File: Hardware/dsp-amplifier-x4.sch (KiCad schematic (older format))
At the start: 35 parts, among them J1 Raspberry_Pi_2_3, J3 USBi, P1 Conn_WallPlug_Earth, Q1 STD2805, U1 ADAU1452

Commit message: various fixes
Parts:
- added C42, C43, C44, C48, C49, C50, C55, C57, C60, C61: 10n, Capacitor_SMD:C_0805_2012Metric_Pad1.18x1.45mm_HandSolder, symbol dsp-amplifier-x4-rescue:Capacitor
- added C45, C46, C47, C51, C52, C53, C58, C59, C62, C63: 100n, Capacitor_SMD:C_0805_2012Metric_Pad1.18x1.45mm_HandSolder, symbol dsp-amplifier-x4-rescue:Capacitor
- added J4, J5: Screw_Terminal_01x02, TerminalBlock:TerminalBlock_Altech_AK300-2_P5.00mm, symbol Connector:Screw_Terminal_01x02
- added R38, R39, R40: 33, Resistor_SMD:R_0603_1608Metric_Pad0.98x0.95mm_HandSolder, symbol Device:R
- added R41, R44: 4.3k, Resistor_SMD:R_0603_1608Metric_Pad0.98x0.95mm_HandSolder, symbol Device:R
- added R42, R43: DNP, Resistor_SMD:R_0603_1608Metric_Pad0.98x0.95mm_HandSolder, symbol Device:R
- added RV1, RV2: R_POT, Potentiometer_THT:Potentiometer_Vishay_248GJ-249GJ_Single_Vertical, symbol Device:R_POT
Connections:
- net labels added: AMP1_BCLK, AMP1_NSPK_SD, AMP1_SPK_SLEEP, AMP2_BCLK, AMP2_NSPK_SD, AMP2_SPK_SLEEP, EXT_I_BCLK, EXT_I_SDATA, EXT_O_BCLK, EXT_O_LRCLK, EXT_O_SDIN, GAIN0, GAIN1, VDRIVE, VPOT0, VPOT1
- net labels removed: AMP1_SCLK, AMP2_SCLK
- wire segments 171 -> 294
- no-connect marks 15 -> 18
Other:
- moved on the sheet: C21, C22, C23, C24, C28, FB1, J1, Q1, R1, R9

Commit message: started routing
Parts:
- removed C42, C43, C48, C49, C50, C55, C57, C60, C61: 10n, Capacitor_SMD:C_0805_2012Metric_Pad1.18x1.45mm_HandSolder, symbol dsp-amplifier-x4-rescue:Capacitor
- removed C45, C46, C51, C52, C53, C58, C59, C62, C63: 100n, Capacitor_SMD:C_0805_2012Metric_Pad1.18x1.45mm_HandSolder, symbol dsp-amplifier-x4-rescue:Capacitor
- removed P1: Conn_WallPlug_Earth, symbol Connector:Conn_WallPlug_Earth
- removed R16, R38, R39: 33, Resistor_SMD:R_0603_1608Metric_Pad0.98x0.95mm_HandSolder, symbol Device:R
- added C10, C11, C14, C15, C16, C20, C21, C3, C4: 10n, Capacitor_SMD:C_0603_1608Metric_Pad1.08x0.95mm_HandSolder, symbol Device:C
- added C12, C13, C17, C18, C19, C23, C24, C7, C8: 100n, Capacitor_SMD:C_0603_1608Metric_Pad1.08x0.95mm_HandSolder, symbol Device:C
- added F1: Fuse, Fuse:Fuseholder_Cylinder-5x20mm_Stelvio-Kontek_PTF78_Horizontal_Open, symbol Device:Fuse
- added J2: EXT, Connector_PinHeader_2.54mm:PinHeader_2x08_P2.54mm_Vertical, symbol Connector_Generic:Conn_02x08_Odd_Even
- added J6, J7: Screw_Terminal_01x02, TerminalBlock:TerminalBlock_Wuerth_691311400102_P7.62mm, symbol Connector:Screw_Terminal_01x02
- added P1: Conn_WallPlug, symbol Connector:Conn_WallPlug
- added R23, R24, R25, R26: 33, Resistor_SMD:R_0603_1608Metric_Pad0.98x0.95mm_HandSolder, symbol Device:R
- C1: renamed from C21; value 4.7u -> 10u; footprint Capacitor_SMD:C_0805_2012Metric_Pad1.18x1.45mm_HandSolder -> Capacitor_SMD:C_1206_3216Metric_Pad1.33x1.80mm_HandSolder; symbol dsp-amplifier-x4-rescue:Capacitor -> Device:C
- C22: renamed from C23; value 4.7u -> 10u; footprint Capacitor_SMD:C_0805_2012Metric_Pad1.18x1.45mm_HandSolder -> Capacitor_SMD:C_1206_3216Metric_Pad1.33x1.80mm_HandSolder; symbol dsp-amplifier-x4-rescue:Capacitor -> Device:C
- C25: renamed from C24; value 4.7u -> 10u; footprint Capacitor_SMD:C_0805_2012Metric_Pad1.18x1.45mm_HandSolder -> Capacitor_SMD:C_1206_3216Metric_Pad1.33x1.80mm_HandSolder; symbol dsp-amplifier-x4-rescue:Capacitor -> Device:C
- C26: renamed from C28; value 4.7u -> 10u; footprint Capacitor_SMD:C_0805_2012Metric_Pad1.18x1.45mm_HandSolder -> Capacitor_SMD:C_1206_3216Metric_Pad1.33x1.80mm_HandSolder; symbol dsp-amplifier-x4-rescue:Capacitor -> Device:C
- C27: renamed from C22; value 4.7u -> 10u; footprint Capacitor_SMD:C_0805_2012Metric_Pad1.18x1.45mm_HandSolder -> Capacitor_SMD:C_1206_3216Metric_Pad1.33x1.80mm_HandSolder; symbol dsp-amplifier-x4-rescue:Capacitor -> Device:C
- C5: renamed from C44; footprint Capacitor_SMD:C_0805_2012Metric_Pad1.18x1.45mm_HandSolder -> Capacitor_SMD:C_0603_1608Metric_Pad1.08x0.95mm_HandSolder; symbol dsp-amplifier-x4-rescue:Capacitor -> Device:C
- C9: renamed from C47; footprint Capacitor_SMD:C_0805_2012Metric_Pad1.18x1.45mm_HandSolder -> Capacitor_SMD:C_0603_1608Metric_Pad1.08x0.95mm_HandSolder; symbol dsp-amplifier-x4-rescue:Capacitor -> Device:C
- FB1: footprint Inductor_SMD:L_0805_2012Metric_Pad1.05x1.20mm_HandSolder -> Inductor_SMD:L_0603_1608Metric_Pad1.05x0.95mm_HandSolder
- J4, J5: footprint TerminalBlock:TerminalBlock_Altech_AK300-2_P5.00mm -> TerminalBlock:TerminalBlock_Wuerth_691311400102_P7.62mm
- renumbered C19 to C2, C20 to C6, J3 to J1, J1 to J3, R14 to R1, R25 to R10, R26 to R11, R27 to R12, R9 to R13, R28 to R14, R32 to R15, R33 to R16, R34 to R17, R35 to R18, R36 to R19, R15 to R2, R29 to R20, R30 to R21, R31 to R22, R41 to R27, R42 to R28, R43 to R29, R17 to R3, R44 to R30, R1 to R4, R21 to R5, R40 to R6, R22 to R7, R23 to R8, R24 to R9
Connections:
- net labels added: EXT_BCLK, EXT_LRCLK, EXT_MCLK, EXT_MDI, EXT_MDO, SCL, SDA
- net labels removed: EXT_I_BCLK, EXT_I_SDATA, EXT_O_BCLK, EXT_O_LRCLK, EXT_O_SDIN
- wire segments 294 -> 334
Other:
- moved on the sheet: C2, C6, FB1, J1, J3, J4, J5, Q1, R1, R13, R14, R15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

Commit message: routing progress
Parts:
- removed R21: 33, Resistor_SMD:R_0603_1608Metric_Pad0.98x0.95mm_HandSolder, symbol Device:R
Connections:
- net AMP1_CLOCK: now also R25.2; no longer R23.2
- net DSP_CLOCK: now also R23.2; no longer R25.2
- net PI_SDATA_I: now also J3.38 (GPIO20/MOSI1)
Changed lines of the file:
@@
 PI_SDATA_I
-Wire Wire Line
-	8000 7550 8700 7550
 Wire Wire Line
 	9600 1000 9350 1000
@@
 Text Label 11550 2050 2    60   ~ 0
 AMP2_CLOCK
+Text Label 11550 2250 2    60   ~ 0
+AMP1_CLOCK
 Text Label 11550 1850 2    60   ~ 0
-AMP1_CLOCK
-Text Label 11550 2250 2    60   ~ 0
 DSP_CLOCK
 Wire Wire Line
@@
 $EndComp
 $Comp
-L Device:R R21
-U 1 1 60BB796A
-P 8850 7550
-F 0 "R21" V 8643 7550 50  0001 C CNN
-F 1 "33" V 8734 7550 50  0001 C CNN
-F 2 "Resistor_SMD:R_0603_1608Metric_Pad0.98x0.95mm_HandSolder" V 8780 7550 50  0001 C CNN
-F 3 "~" H 8850 7550 50  0001 C CNN
-	1    8850 7550
-	0    1    1    0
-$EndComp
-$Comp
 L Device:R R22
 U 1 1 60BB7970
@@
 Wire Wire Line
 	9000 7450 9050 7450
-Wire Wire Line
-	9050 7550 9000 7550
 Wire Wire Line
 	9000 7650 9050 7650
@@
 Wire Wire Line
 	10550 2050 10500 2050
+Wire Wire Line
+	8000 7550 9050 7550
 $EndSCHEMATC

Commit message: routing, added 4 layers
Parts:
- J3: footprint Connector_PinHeader_2.54mm:PinHeader_2x20_P2.54mm_Vertical -> rpi_socket:PinSocket_2x20_P2.54mm_Vertical
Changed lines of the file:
@@
 F 0 "J3" H 9850 9131 50  0000 C CNN
 F 1 "Raspberry_Pi_2_3" H 9850 9040 50  0000 C CNN
-F 2 "Connector_PinHeader_2.54mm:PinHeader_2x20_P2.54mm_Vertical" H 9850 7650 50  0001 C CNN
+F 2 "rpi_socket:PinSocket_2x20_P2.54mm_Vertical" H 9850 7650 50  0001 C CNN
 F 3 "https://www.raspberrypi.org/documentation/hardware/raspberrypi/schematics/rpi_SCH_3bplus_1p0_reduced.pdf" H 9850 7650 50  0001 C CNN
 	1    9850 7650
@@
 Text Label 8000 7450 0    60   ~ 0
 PI_LRCLK
-Text Label 8350 7250 0    60   ~ 0
-PI_BCLK
 Text Label 8000 7650 0    60   ~ 0
 PI_SDATA_O
@@
 	10150 9000 10150 8950
 Connection ~ 10050 9000
-$Comp
-L power:+5VD #PWR033
-U 1 1 6086659C
-P 9650 6050
-F 0 "#PWR033" H 9650 5900 50  0001 C CNN
-F 1 "+5VD" H 9665 6223 50  0000 C CNN
-F 2 "" H 9650 6050 50  0001 C CNN
-F 3 "" H 9650 6050 50  0001 C CNN
-	1    9650 6050
-	1    0    0    -1
-$EndComp
-Wire Wire Line
-	9650 6050 9650 6300
 Wire Wire Line
 	9750 6350 9750 6300
 Wire Wire Line
 	9750 6300 9650 6300
-Connection ~ 9650 6300
 Wire Wire Line
 	9650 6300 9650 6350
@@
 Text Label 8350 8350 0    60   ~ 0
 PI_MUTE
-Text Label 8350 7150 0    60   ~ 0
-DSP_NRESET
 Text Label 8350 8150 0    60   ~ 0
 DSP_SELFBOOT
@@
 	1400 4550 2600 4550
 Wire Wire Line
-	8350 7150 9050 7150
-Wire Wire Line
-	8350 7250 9050 7250
-Wire Wire Line
 	8000 7450 8700 7450
 Wire Wire Line
@@
 Wire Wire Line
 	8000 7550 9050 7550
+Wire Wire Line
+	8350 7250 9050 7250
+Wire Wire Line
+	8350 7150 9050 7150
+Text Label 8350 7150 0    60   ~ 0
+DSP_NRESET
+Text Label 8350 7250 0    60   ~ 0
+PI_BCLK
+Connection ~ 9650 6300
+$Comp
+L power:+5VD #PWR033
+U 1 1 6086659C
+P 9650 6050
+F 0 "#PWR033" H 9650 5900 50  0001 C CNN
+F 1 "+5VD" H 9665 6223 50  0000 C CNN
+F 2 "" H 9650 6050 50  0001 C CNN
+F 3 "" H 9650 6050 50  0001 C CNN
+	1    9650 6050
+	1    0    0    -1
+$EndComp
+Wire Wire Line
+	9650 6050 9650 6300
 $EndSCHEMATC

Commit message: complete
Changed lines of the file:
@@
 PI_SDATA_I
-Wire Wire Line
-	9600 1000 9350 1000
 Wire Wire Line
 	9350 1000 9350 950
@@
 	14050 1400 14050 1350
 Connection ~ 14050 1350
-$Comp
-L Device:Fuse F1
-U 1 1 607081C8
-P 9750 1000
-F 0 "F1" V 9553 1000 50  0000 C CNN
-F 1 "Fuse" V 9644 1000 50  0000 C CNN
-F 2 "Fuse:Fuseholder_Cylinder-5x20mm_Stelvio-Kontek_PTF78_Horizontal_Open" V 9680 1000 50  0001 C CNN
-F 3 "~" H 9750 1000 50  0001 C CNN
-	1    9750 1000
-	0    1    1    0
-$EndComp
-Wire Wire Line
-	9950 1000 9900 1000
-Wire Wire Line
-	9350 1100 9950 1100
 $Sheet
 S 13050 4000 1400 1400
@@
 Wire Wire Line
 	9650 6050 9650 6300
+Wire Wire Line
+	9950 1000 9900 1000
+$Comp
+L Device:Fuse F1
+U 1 1 607081C8
+P 9750 1000
+F 0 "F1" V 9553 1000 50  0000 C CNN
+F 1 "Fuse" V 9644 1000 50  0000 C CNN
+F 2 "Fuse:Fuseholder_Cylinder-5x20mm_Stelvio-Kontek_PTF78_Horizontal_Open" V 9680 1000 50  0001 C CNN
+F 3 "~" H 9750 1000 50  0001 C CNN
+	1    9750 1000
+	0    1    1    0
+$EndComp
+Wire Wire Line
+	9350 1000 9600 1000
+Wire Wire Line
+	9950 1100 9350 1100
 $EndSCHEMATC

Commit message: bugfixes, made smaller
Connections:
- no-connect marks 18 -> 22
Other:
- note added: "GAIN[1:0]\n00: 12.9 V full-scale\n01: 15.1 V full-scale\n10: 25.15 V full-scale\n11: Software-controlled"
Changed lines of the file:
@@
 Wire Wire Line
 	9950 1100 9350 1100
+NoConn ~ 10500 1750
+NoConn ~ 10500 1950
+NoConn ~ 10500 2150
+NoConn ~ 10500 2350
+Text Notes 14450 1100 0    60   ~ 0
+GAIN[1:0]\n00: 12.9 V full-scale\n01: 15.1 V full-scale\n10: 25.15 V full-scale\n11: Software-controlled
 $EndSCHEMATC

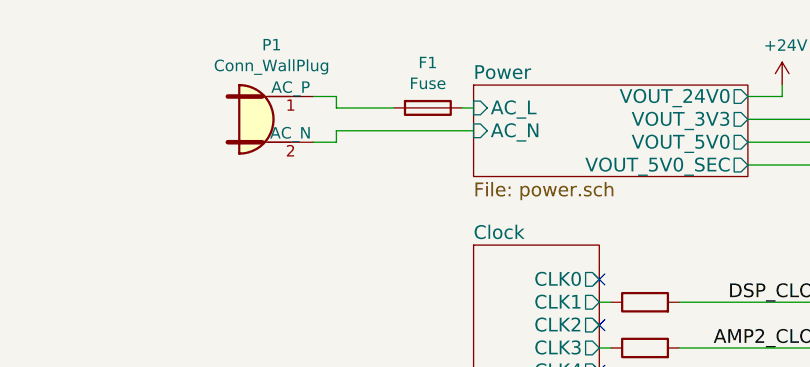
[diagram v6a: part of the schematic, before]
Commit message: connector for ac
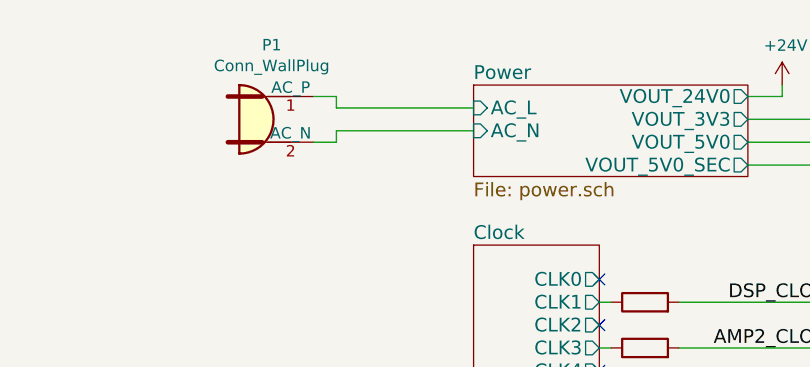
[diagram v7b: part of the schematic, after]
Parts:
- removed F1: Fuse, Fuse:Fuseholder_Cylinder-5x20mm_Stelvio-Kontek_PTF78_Horizontal_Open, symbol Device:Fuse
- P1: footprint (none) -> TerminalBlock:TerminalBlock_Wuerth_691311400102_P7.62mm
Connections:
- net Power/AC_L: now also P1.1 (AC_P)
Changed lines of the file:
@@
 F 0 "P1" H 9067 1375 50  0000 C CNN
 F 1 "Conn_WallPlug" H 9067 1284 50  0000 C CNN
-F 2 "" H 9450 1050 50  0001 C CNN
+F 2 "TerminalBlock:TerminalBlock_Wuerth_691311400102_P7.62mm" H 9450 1050 50  0001 C CNN
 F 3 "~" H 9450 1050 50  0001 C CNN
 	1    9050 1050
@@
 	9650 6050 9650 6300
 Wire Wire Line
-	9950 1000 9900 1000
-$Comp
-L Device:Fuse F1
-U 1 1 607081C8
-P 9750 1000
-F 0 "F1" V 9553 1000 50  0000 C CNN
-F 1 "Fuse" V 9644 1000 50  0000 C CNN
-F 2 "Fuse:Fuseholder_Cylinder-5x20mm_Stelvio-Kontek_PTF78_Horizontal_Open" V 9680 1000 50  0001 C CNN
-F 3 "~" H 9750 1000 50  0001 C CNN
-	1    9750 1000
-	0    1    1    0
-$EndComp
-Wire Wire Line
-	9350 1000 9600 1000
-Wire Wire Line
 	9950 1100 9350 1100
 NoConn ~ 10500 1750
@@
 Text Notes 14450 1100 0    60   ~ 0
 GAIN[1:0]\n00: 12.9 V full-scale\n01: 15.1 V full-scale\n10: 25.15 V full-scale\n11: Software-controlled
+Wire Wire Line
+	9350 1000 9950 1000
 $EndSCHEMATC

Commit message: style fixes, spi/i2c
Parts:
- removed R15, R16, R18: 4.3k, Resistor_SMD:R_0603_1608Metric_Pad0.98x0.95mm_HandSolder, symbol Device:R
- removed R17, R19: 4.3k DNP, Resistor_SMD:R_0603_1608Metric_Pad0.98x0.95mm_HandSolder, symbol Device:R
- R14: value 4.3k -> 33
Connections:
- net DSP_ADDR0 is gone; now on net PI_NCE0: U1.33 (SS/ADDR0)
- net DSP_ADDR1 is gone; now on net PI_MOSI0: U1.32 (MOSI/ADDR1)
- net +3V3: no longer R14.2
- net AMP1_NSPK_SD: now also U1.39 (LRCLK_OUT0/MP4); no longer U1.26 (SS_M/MP0)
- net AMP1_SPK_SLEEP: now also U1.42 (LRCLK_OUT1/MP5); no longer U1.27 (MOSI_M/MP1)
- net DSP_SELFBOOT: now also J3.15 (GPIO22); no longer J3.22 (GPIO25)
- net PI_BCLK: now also R14.2; no longer J3.12 (GPIO18/PWM0)
- net PI_MISO0: now also J1.5 (Pin_5), U1.30 (MISO/SDA)
- net PI_MOSI0: now also J1.8 (Pin_8)
- net PI_MUTE: now also U1.69 (LRCLK_IN3/MP13)
- net PI_NCE0: now also J1.9 (Pin_9)
- net PI_SCLK0: now also J1.7 (Pin_7), U1.31 (SCLK/SCL)
- net EEPROM_SCL: no longer names the net of R14.1
- net EEPROM_SCL: now also J3.12 (GPIO18/PWM0); no longer U1.28 (SCL_M/SCLK_M/MP2)
- net EEPROM_SDA renamed EEPROM_MISO
- net PI_NCE1: no longer names the net of J3.26 (~CE1~/GPIO7)
- net PI_SCL: no longer names the net of J3.5 (SCL/GPIO3)
- net PI_SDA: no longer names the net of J3.3 (SDA/GPIO2)
- removed net SCL: J1.1 (Pin_1), J2.13 (Pin_13), U1.31 (SCLK/SCL)
- removed net SDA: J1.3 (Pin_3), J2.11 (Pin_11), U1.30 (MISO/SDA)
- new net EEPROM_MOSI: U1.27 (MOSI_M/MP1)
- new net EEPROM_NCS: U1.26 (SS_M/MP0)
- new net EEPROM_SCK: U1.28 (SCL_M/SCLK_M/MP2)
- no-connect marks 22 -> 33
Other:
- moved on the sheet: J1
